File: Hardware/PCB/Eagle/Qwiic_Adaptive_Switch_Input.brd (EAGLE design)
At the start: 43.2 x 38.1 mm, 59 parts, among them J1 QWIIC_RIGHT_ANGLE, J4 QWIIC_RIGHT_ANGLE, SW1 CUI_SJ1-3513, SW2 CUI_SJ1-3513, U1 TCA9534

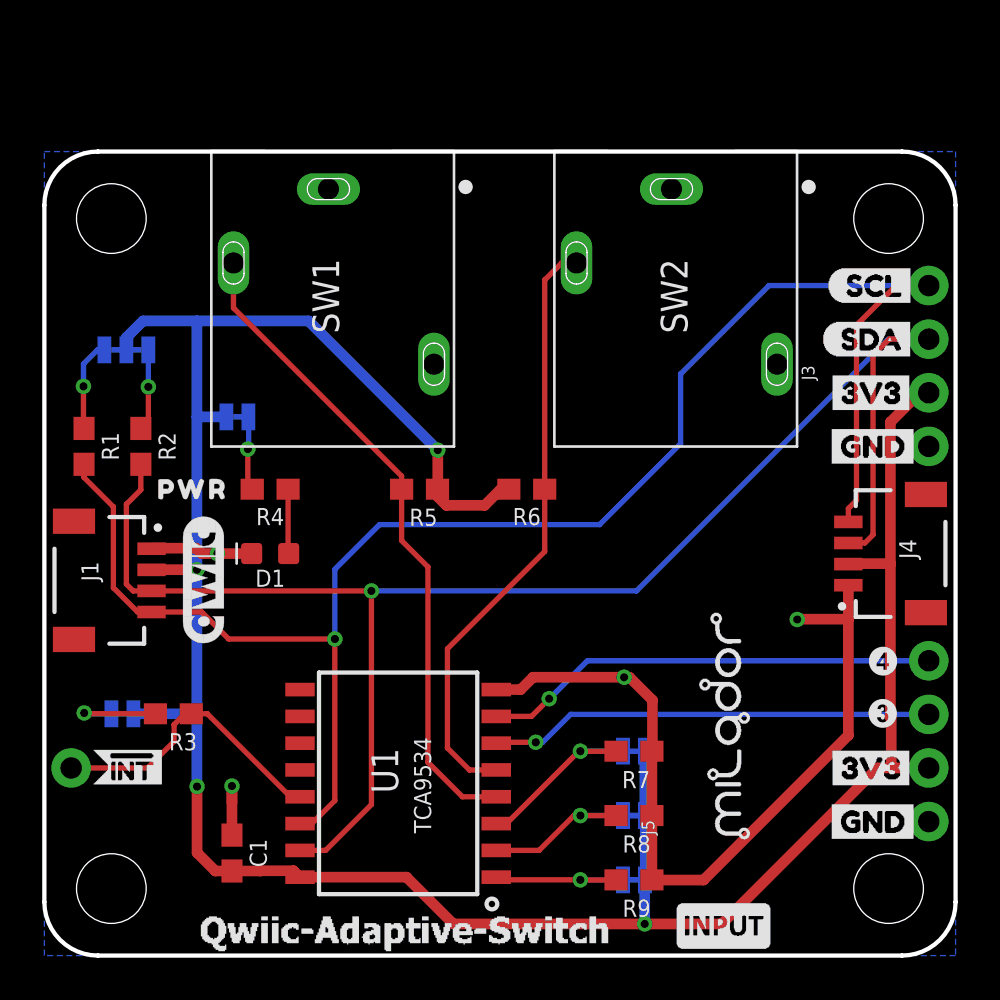
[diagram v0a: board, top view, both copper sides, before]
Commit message: Updated PCB Designs to match input with output designs
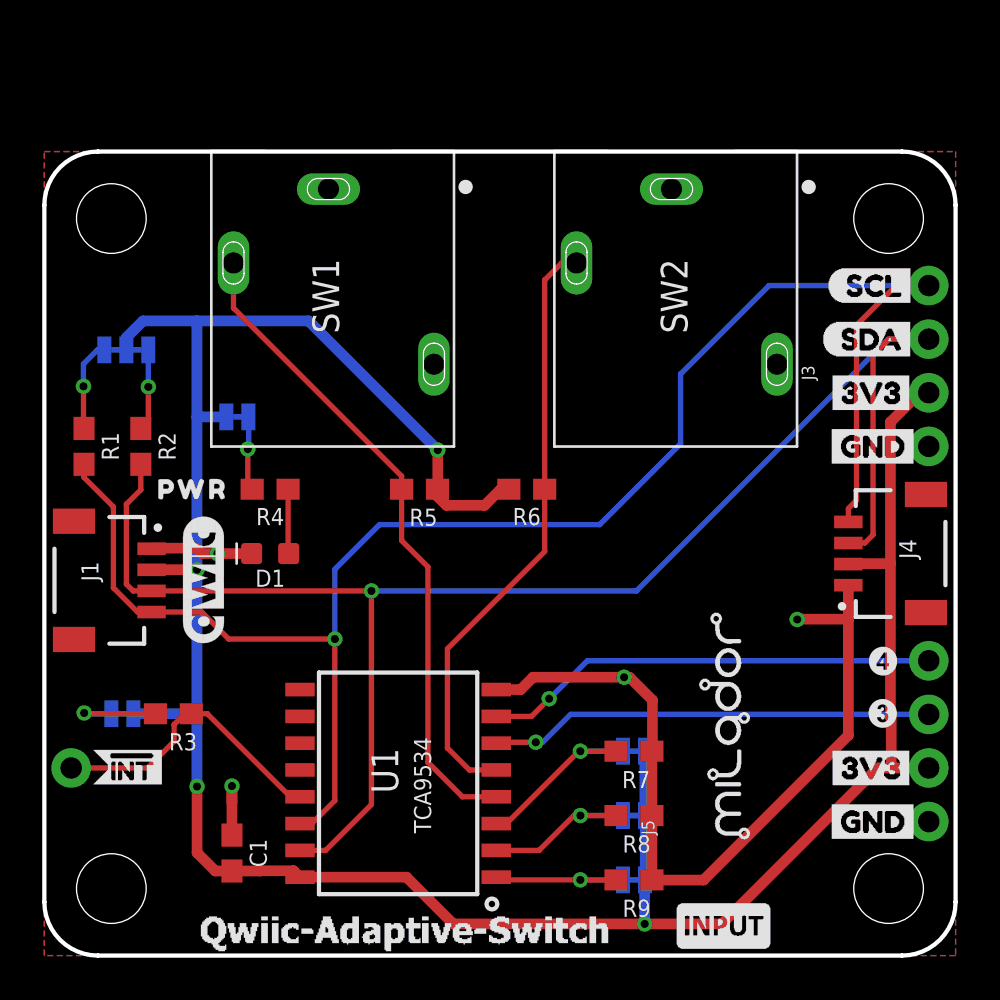
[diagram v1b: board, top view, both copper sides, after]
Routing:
- added copper zone on layer 1, net GND
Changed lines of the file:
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@@
 <drawing>
 <settings>
-<setting alwaysvectorfont="yes"/>
+<setting alwaysvectorfont="no"/>
 <setting keepoldvectorfont="yes"/>
 <setting verticaltext="up"/>
 </settings>
-<grid distance="1.2" unitdist="mil" unit="mm" style="lines" multiple="1" display="yes" altdistance="0.005" altunitdist="inch" altunit="inch"/>
+<grid distance="1" unitdist="mm" unit="mm" style="lines" multiple="1" display="yes" altdistance="0.005" altunitdist="inch" altunit="inch"/>
 <layers>
 <layer number="1" name="Top" color="4" fill="1" visible="yes" active="yes"/>
@@
 <wire x1="38.1" y1="15.9410375" x2="35.692078125" y2="15.9410375" width="0.508" layer="1"/>
 <wire x1="35.676840625" y1="15.9258" x2="35.692078125" y2="15.9410375" width="0.508" layer="1"/>
+<polygon width="0.2032" layer="1" isolate="0.3048">
+<vertex x="0" y="38.1"/>
+<vertex x="43.18" y="38.1"/>
+<vertex x="43.18" y="0"/>
+<vertex x="0" y="0"/>
+</polygon>
 </signal>
 <signal name="SCL_PU1">

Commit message: Updated PCB Mount holes
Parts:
- H1, H2: value STAND-OFF -> STAND-OFF-3.3; device SparkFun-Hardware:STAND-OFF -> milador:STAND-OFF-3.3
- JP3, JP4: value STAND-OFF -> STAND-OFF-3.3; device SparkFun:STAND-OFF -> milador:STAND-OFF-3.3
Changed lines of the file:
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@@
 </autorouter>
 <elements>
-<element name="JP3" library="SparkFun" package="STAND-OFF" value="STAND-OFF" x="3.175" y="3.175" smashed="yes"/>
-<element name="JP4" library="SparkFun" package="STAND-OFF" value="STAND-OFF" x="40.005" y="3.175" smashed="yes"/>
+<element name="JP3" library="milador" library_urn="urn:adsk.eagle:library:12595918" package="STAND-OFF-3.3" package3d_urn="urn:adsk.eagle:package:30775189/1" value="STAND-OFF-3.3" x="3.175" y="3.175" smashed="yes"/>
+<element name="JP4" library="milador" library_urn="urn:adsk.eagle:library:12595918" package="STAND-OFF-3.3" package3d_urn="urn:adsk.eagle:package:30775189/1" value="STAND-OFF-3.3" x="40.005" y="3.175" smashed="yes"/>
 <element name="J1" library="milador_SMD" library_urn="urn:adsk.eagle:library:27847482" package="CONNECTORS_JST04_1MM_RA" package3d_urn="urn:adsk.eagle:package:29222212/3" value="QWIIC_RIGHT_ANGLE" x="5.08" y="17.78" smashed="yes" rot="R270">
 <attribute name="NAME" x="1.7526" y="18.669" size="0.8128" layer="21" font="vector" ratio="15" rot="R270"/>
@@
 <element name="LABEL_28" library="buzzard_labels (44)" package="GND4" value="" x="41.656" y="24.13" smashed="yes" rot="MR0"/>
 <element name="LABEL_27" library="buzzard_labels (44)" package="3V33" value="" x="41.529" y="26.67" smashed="yes" rot="MR0"/>
-<element name="H1" library="SparkFun-Hardware" package="STAND-OFF" value="STAND-OFF" x="40.005" y="34.925" smashed="yes">
-<attribute name="VALUE" x="40.005" y="32.893" size="0.6096" layer="27" font="vector" ratio="20" align="top-center"/>
-</element>
-<element name="H2" library="SparkFun-Hardware" package="STAND-OFF" value="STAND-OFF" x="3.175" y="34.925" smashed="yes"/>
+<element name="H1" library="milador" library_urn="urn:adsk.eagle:library:12595918" package="STAND-OFF-3.3" package3d_urn="urn:adsk.eagle:package:30775189/1" value="STAND-OFF-3.3" x="40.005" y="34.925" smashed="yes"/>
+<element name="H2" library="milador" library_urn="urn:adsk.eagle:library:12595918" package="STAND-OFF-3.3" package3d_urn="urn:adsk.eagle:package:30775189/1" value="STAND-OFF-3.3" x="3.175" y="34.925" smashed="yes"/>
 <element name="R3" library="milador_SMD" library_urn="urn:adsk.eagle:library:27847482" package="0603" package3d_urn="urn:adsk.eagle:package:29222124/2" value="10k" x="6.11378125" y="11.4587" smashed="yes" rot="R180">
 <attribute name="NAME" x="6.57098125" y="10.53921875" size="0.8128" layer="21" font="vector" ratio="15" rot="R180" align="bottom-center"/>

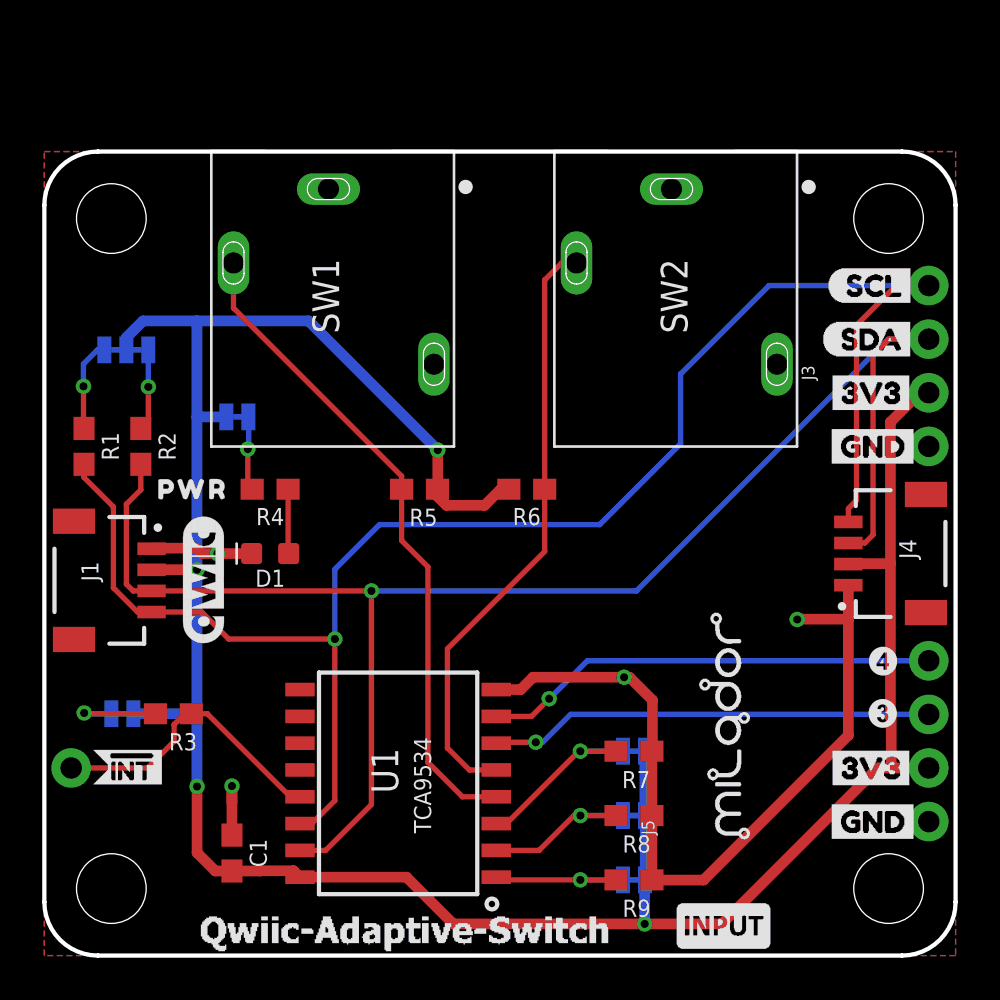
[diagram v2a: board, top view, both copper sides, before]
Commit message: Updated footprints to 0805 packages
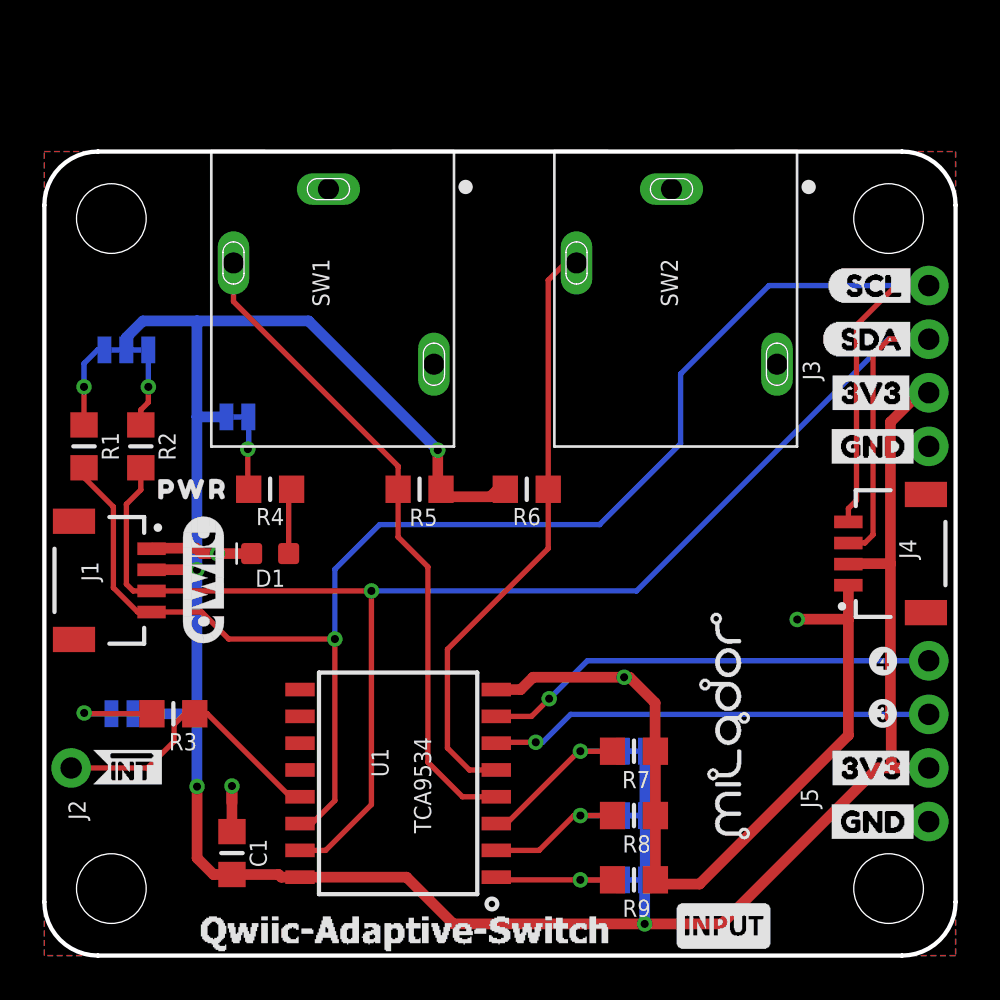
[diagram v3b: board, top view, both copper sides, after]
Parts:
- C1, R1, R2, R3, R4, R5, R6, R7, R8, R9: device milador_SMD:0603 -> milador_SMD:0805-MP
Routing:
- net 3.3V: track 124.3 -> 123.7 mm

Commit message: Updated silkscreen
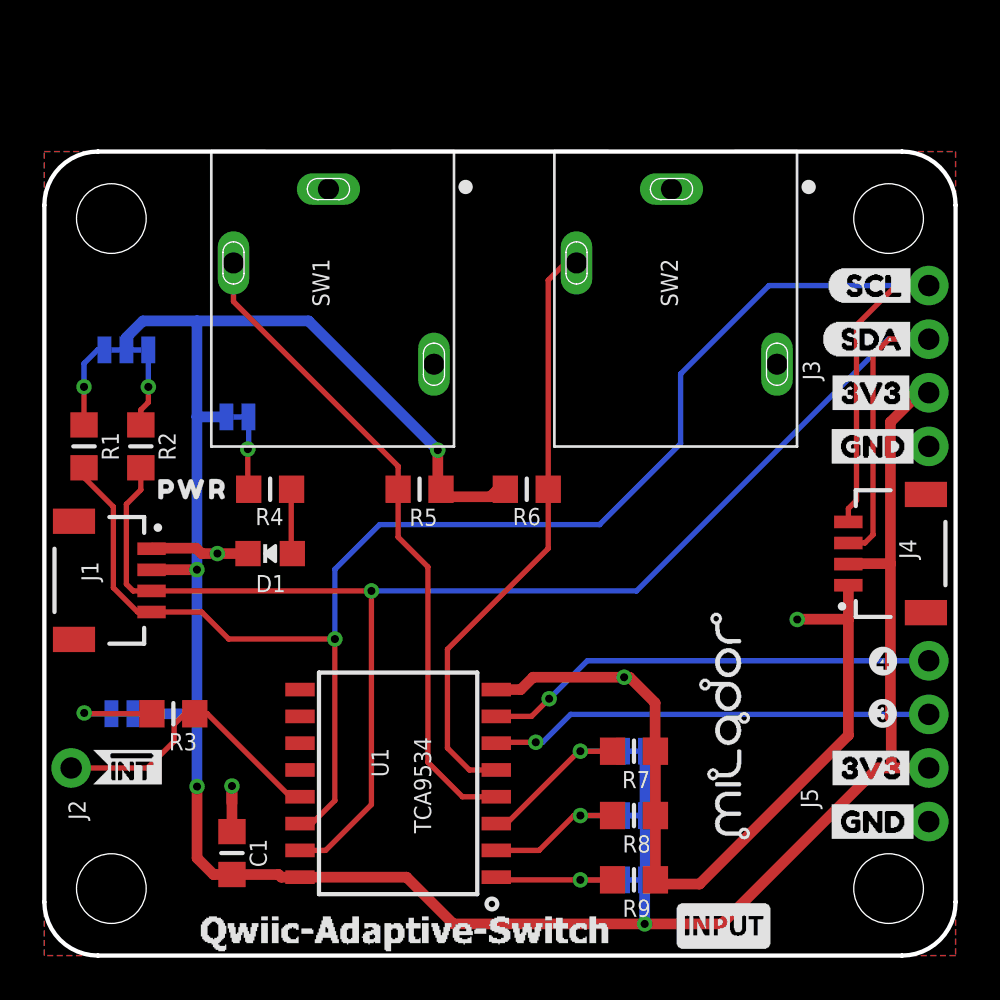
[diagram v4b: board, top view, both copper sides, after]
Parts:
- removed LABEL_6: (no value), SparkFun-Aesthetics:QWIIC_6MM
- D1: device milador_SMD:LED-0603 -> milador_SMD:CHIPLED_0805_NOOUTLINE
- turned D1 to 90 degrees

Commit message: Updated design to version 1.2
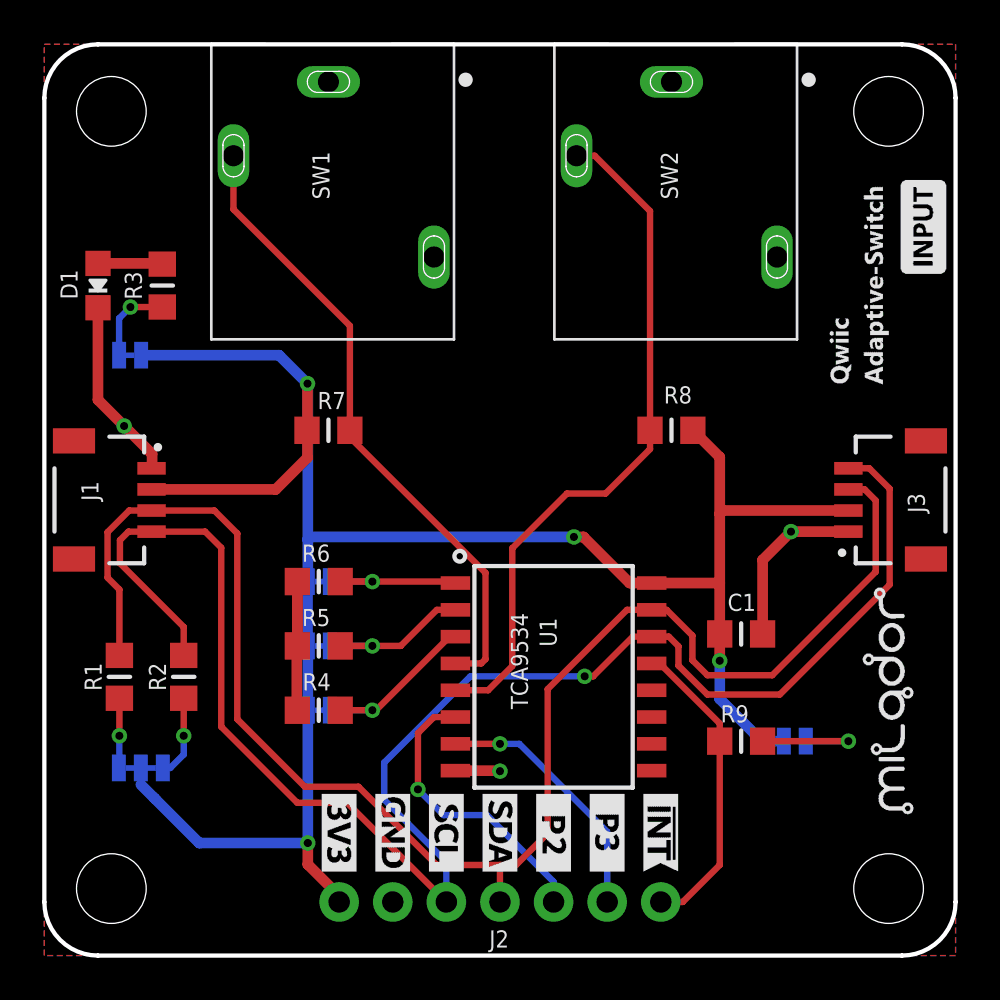
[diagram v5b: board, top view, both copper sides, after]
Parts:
- removed J4: QWIIC_RIGHT_ANGLE, milador_SMD:CONNECTORS_JST04_1MM_RA
- removed J5: (no value), milador:CONNECTORS_1X04_NO_SILK
- removed LABEL_1: (no value), SparkFun-Buzzard:I2C
- removed LABEL_10: (no value), output:#INT#0
- removed LABEL_11: (no value), buzzard_labels (52):#INT0
- removed LABEL_12: (no value), buzzard_labels (54):#INT0
- removed LABEL_13, LABEL_8: (no value), milador:MILADOR_QWIIC_SWITCH
- removed LABEL_14, LABEL_7: MILADOR-LOGO-, milador:MILADOR_LOGO1
- removed LABEL_15: (no value), output:#ADR2#0
- removed LABEL_16: (no value), output:#ADR1#0
- removed LABEL_17: (no value), output:#ADR0#0
- removed LABEL_18, LABEL_9: MILADOR-SWITCH-NAME-SW-INPUT, milador:SWITCH-INPUT
- removed LABEL_19: (no value), buzzard_labels (44):SCL6
- removed LABEL_2: MILADOR-SWITCH-NAME-SW1, milador:SWITCH-SW1
- removed LABEL_20: (no value), buzzard_labels (44):SDA5
- removed LABEL_21, LABEL_23, LABEL_27, LABEL_29: (no value), buzzard_labels (44):3V33
- removed LABEL_22, LABEL_24, LABEL_28, LABEL_30: (no value), buzzard_labels (44):GND4
- removed LABEL_25: (no value), buzzard_labels (51):SCL0
- removed LABEL_26: (no value), buzzard_labels (51):SDA1
- removed LABEL_3: MILADOR-SWITCH-NAME-SW2, milador:SWITCH-SW2
- removed LABEL_4: (no value), output:#PWR#0
- removed LABEL_5: (no value), output:PWR0
- added LABEL_!INT_BOTTOM, LABEL_!INT_TOP: MILADOR-LABEL-!INT, milador:LABEL-!INT
- added LABEL_3V_BOTTOM, LABEL_3V_TOP: MILADOR-LABEL-3V, milador:LABEL-3V
- added LABEL_ADR0: MILADOR-LABEL-ADR0, milador:LABEL-ADR0
- added LABEL_ADR1: MILADOR-LABEL-ADR1, milador:LABEL-ADR1
- added LABEL_ADR2: MILADOR-LABEL-ADR2, milador:LABEL-ADR2
- added LABEL_GND_BOTTOM, LABEL_GND_TOP: MILADOR-LABEL-GND, milador:LABEL-GND
- added LABEL_I2C: MILADOR-LABEL-I2C, milador:LABEL-I2C
- added LABEL_I2C_ADDRESS: MILADOR-LABEL-ADDRESS-0X27, milador:LABEL-ADDRESS-27
- added LABEL_INPUT_BOTTOM, LABEL_INPUT_TOP: MILADOR-SWITCH-NAME-SW-INPUT, milador:SWITCH-INPUT
- added LABEL_INT: MILADOR-LABEL-INT, milador:LABEL-INT
- added LABEL_MILADOR_BOTTOM, LABEL_MILADOR_TOP: MILADOR-LOGO-, milador:MILADOR_LOGO1
- added LABEL_P0_BOTTOM: MILADOR-LABEL-P0, milador:LABEL-P0
- added LABEL_P1_BOTTOM: MILADOR-LABEL-P1, milador:LABEL-P1
- added LABEL_P2_BOTTOM, LABEL_P2_TOP: MILADOR-LABEL-P2, milador:LABEL-P2
- added LABEL_P3_BOTTOM, LABEL_P3_TOP: MILADOR-LABEL-P3, milador:LABEL-P3
- added LABEL_PWR: MILADOR-LABEL-PWR, milador:LABEL-PWR
- added LABEL_SW1: MILADOR-SWITCH-NAME-SW1, milador:SWITCH-SW1
- added LABEL_SW2: MILADOR-SWITCH-NAME-SW2, milador:SWITCH-SW2
- added LABEL_TITLE_BOTTOM: MILADOR-DEVICE-QWIIC-SWITCH, milador:MILADOR_QWIIC_SWITCH
- added LABEL_TITLE_TOP: MILADOR-DEVICE-QWIIC-SWITCH-SM, milador:MILADOR_QWIIC_SWITCH_SM
- added LABE_SCL_BOTTOM, LABE_SCL_TOP: MILADOR-LABEL-SCL, milador:LABEL-SCL
- added LABE_SDA_BOTTOM, LABE_SDA_TOP: MILADOR-LABEL-SDA, milador:LABEL-SDA
- J2: device milador:CONNECTORS_1X01_NO_SILK -> milador:CONNECTORS_1X07_NO_SILK
- J3: value (none) -> QWIIC_RIGHT_ANGLE; device milador:CONNECTORS_1X04_NO_SILK -> milador_SMD:CONNECTORS_JST04_1MM_RA
- R3: value 10k -> 1k
- R4: value 1k -> 2.2k
- R5: value 4.7k -> 2.2k
- R6: value 4.7K -> 2.2k
- R7, R8: value 2.2k -> 4.7K
- R9: value 2.2k -> 10k
- moved INT 31.9 mm to (35.6, 10.2), turned to 0 degrees
- moved C1 26.3 mm to (33.0, 15.2), turned to 0 degrees
- moved R7 21.0 mm to (13.5, 24.9), turned to 0 degrees
- moved ADR0 20.6 mm to (13.0, 17.7), turned to 0 degrees
- moved R3 20.3 mm to (5.59, 31.8), turned to 270 degrees
- moved I2C 19.8 mm to (4.57, 8.89), turned to 180 degrees
- moved R8 18.3 mm to (29.7, 24.9)
- moved ADR1 17.0 mm to (13.0, 14.7), turned to 0 degrees
- moved D1 15.1 mm to (2.54, 31.8), turned to 180 degrees
- moved ADR2 15.1 mm to (13.0, 11.6), turned to 0 degrees
- moved J2 14.2 mm to (14.0, 2.54), turned to 0 degrees
- moved R2 11.1 mm to (6.60, 13.2), turned to 270 degrees
- moved R1 11.0 mm to (3.56, 13.2), turned to 270 degrees
- moved R6 10.8 mm to (13.0, 17.7), turned to 0 degrees
- moved R4 10.7 mm to (13.0, 11.6), turned to 0 degrees
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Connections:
- net !INT: now also J2.7, R9.1; no longer J2.1, R3.1
- net 3.3V: now also J2.1, R7.1, R8.1; no longer J4.2, J5.2, R5.2, R6.2
- net ADR0: now also R6.2; no longer R9.2
- net ADR1: now also R5.2; no longer R8.2
- net ADR2: now also R4.2; no longer R7.2
- net GND: now also J2.2, R4.1, R5.1, R6.1; no longer J4.1, J5.1, R7.1, R8.1, R9.1
- net N$1: now also R9.2; no longer R3.2
- net N$2: now also R3.1; no longer R4.1
- net N$3: now also R3.2; no longer R4.2
- net P0: now also R7.2; no longer R5.1
- net P1: now also R8.2; no longer R6.1
- net P2: now also J2.5; no longer J5.3
- net P3: now also J2.6; no longer J5.4
- net SCL: now also J2.3, R2.1; no longer J4.4, R1.1
- net SCL_PU1: now also R1.2; no longer R2.2
- net SDA: now also J2.4, R1.1; no longer J4.3, R2.1
- net SDA_PU1: now also R2.2; no longer R1.2
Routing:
- net 3.3V: track 123.7 -> 98.8 mm
- net GND: track 46.0 -> 25.1 mm, vias 4 -> 3
- net P3: track 21.6 -> 12.2 mm
- net P2: track 21.1 -> 14.0 mm
- net P1: track 28.6 -> 33.1 mm
- net N$1: track 4.53 -> 6.08 mm
- net SDA: track 76.1 -> 74.7 mm, vias 1 -> 0
- net P0: track 31.4 -> 30.3 mm
- net !INT: track 14.0 -> 14.6 mm
- net SCL: track 80.2 -> 79.6 mm
- net N$3: track 3.51 -> 4.02 mm
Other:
- board size 43.2 x 38.1 mm -> 43.2 x 43.2 mm
